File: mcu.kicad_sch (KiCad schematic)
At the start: 40 parts, among them J17 CAN, J19 Conn_ARM_JTAG_SWD_10, J20 Conn_ARM_JTAG_SWD_10, J21 Conn_01x04_Pin, SW1 RESET, SW2 BOOT, U17 HDC1080, U18 SN65HVD230, U8 STM32G473CBTx, Y1 8 MHz

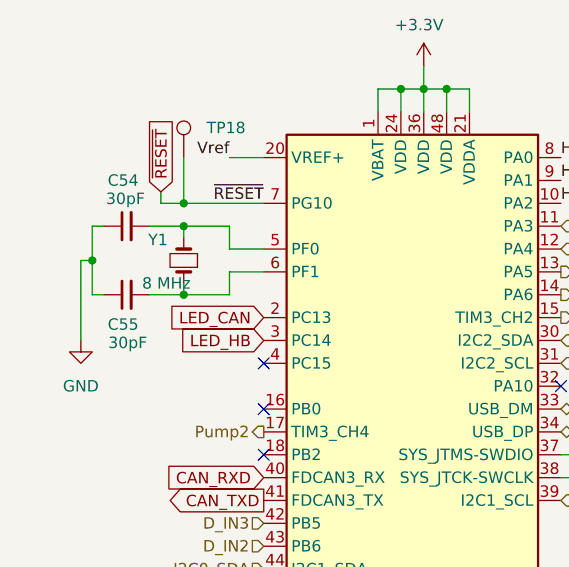
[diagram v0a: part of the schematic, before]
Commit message: Remove 8 MHz crystal
Closes #51
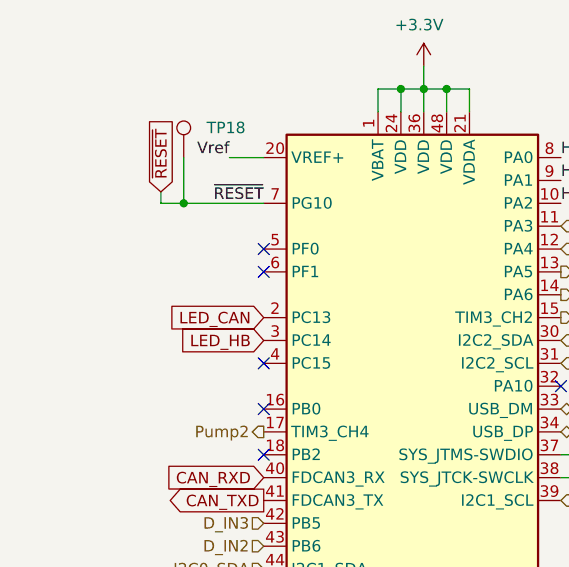
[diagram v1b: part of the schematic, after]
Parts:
- removed C54, C55: 30pF, Capacitor_SMD:C_0603_1608Metric, symbol Device:C_Small
- removed Y1: 8 MHz, Crystal:Crystal_SMD_5032-2Pin_5.0x3.2mm, symbol Device:Crystal_Small
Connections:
- no-connect marks 11 -> 13

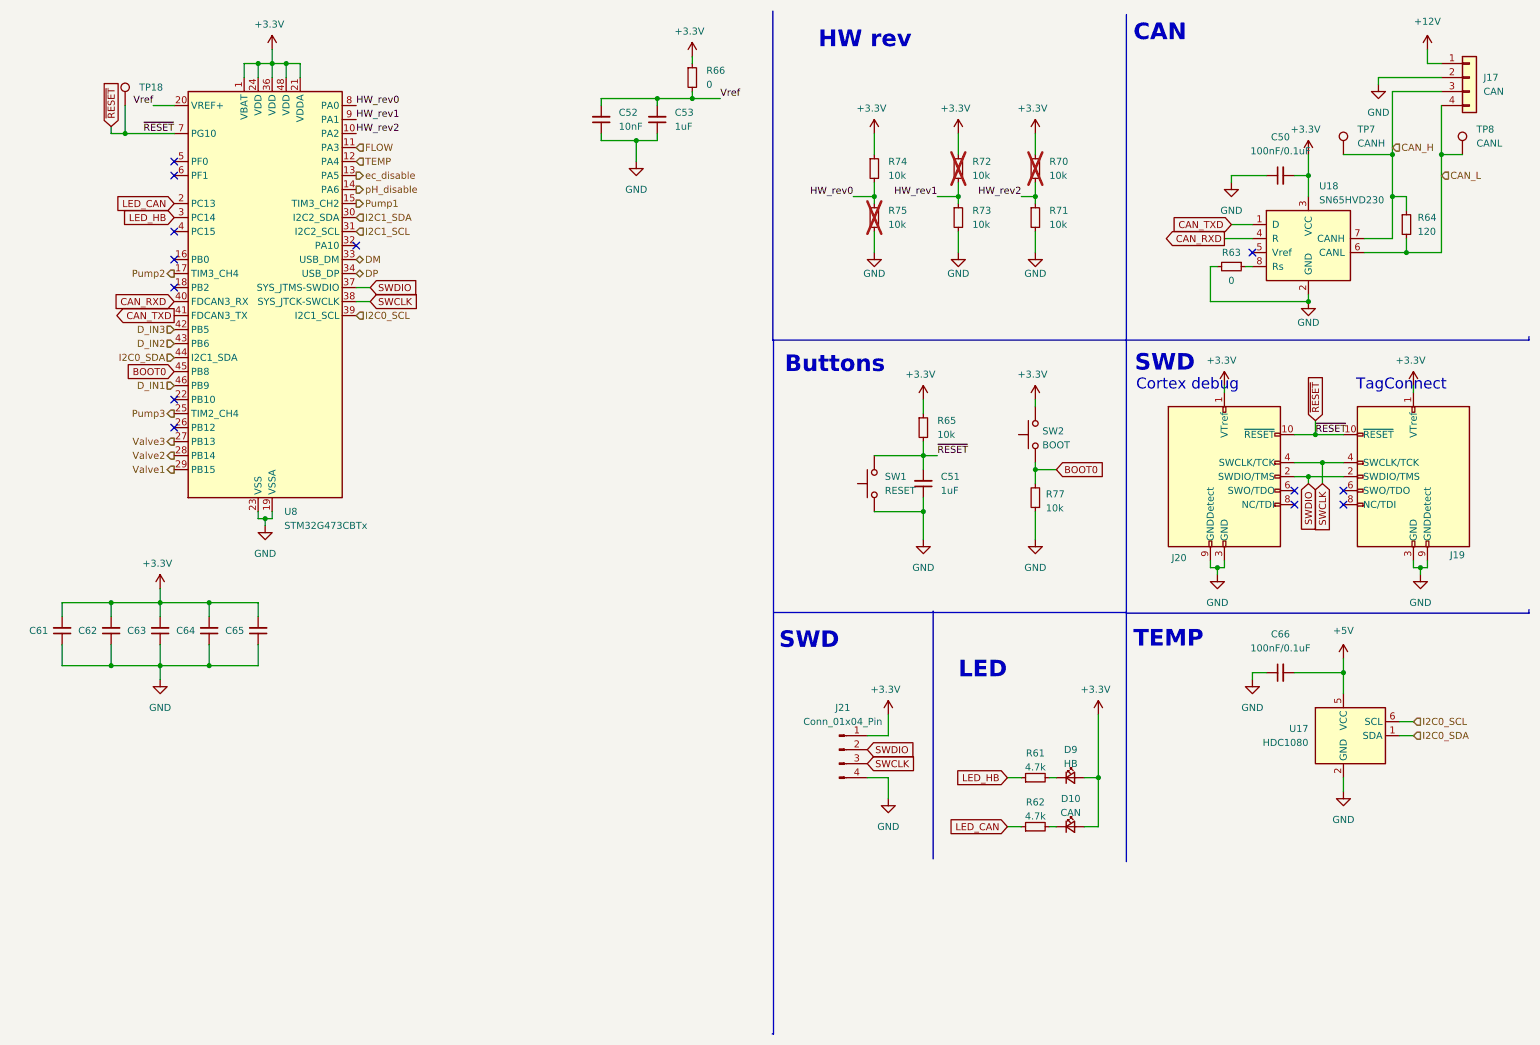
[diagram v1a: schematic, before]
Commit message: Replace MCU with STM32U575RGT
Closes #49
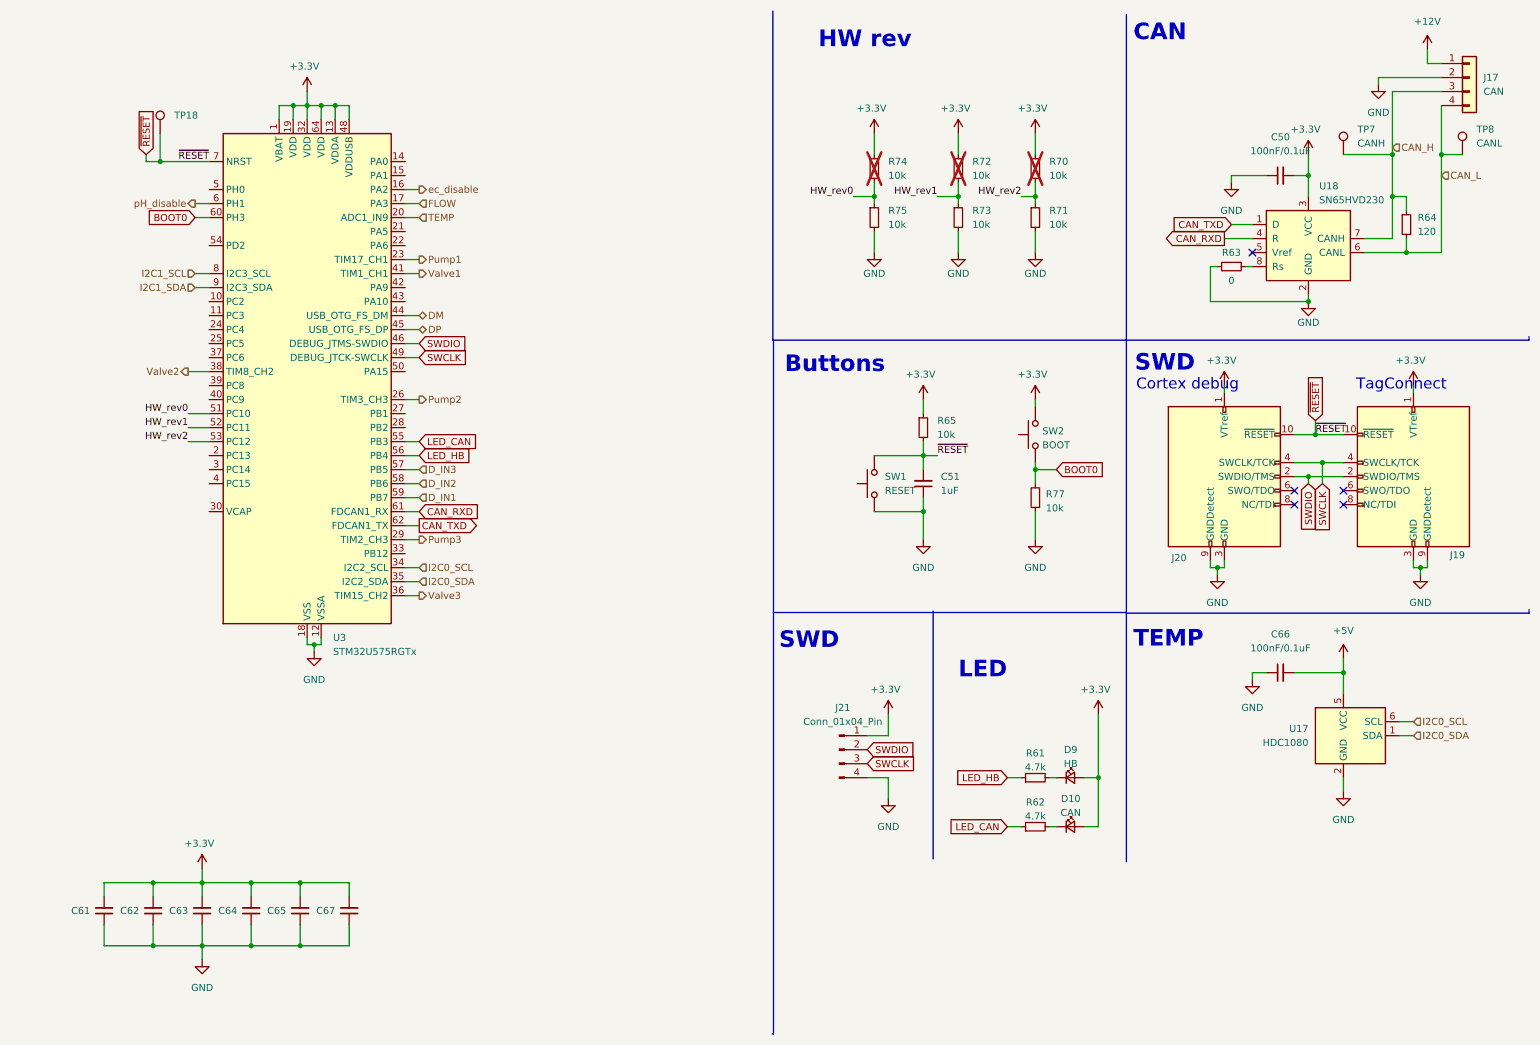
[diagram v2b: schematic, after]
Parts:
- removed C52: 10nF, Capacitor_SMD:C_0402_1005Metric, symbol Device:C_Small
- removed C53: 1uF, Capacitor_SMD:C_0402_1005Metric, symbol Device:C_Small
- removed R66: 0, Resistor_SMD:R_0402_1005Metric, symbol Device:R_Small
- removed U8: STM32G473CBTx, Package_QFP:LQFP-48_7x7mm_P0.5mm, symbol MCU_ST_STM32G4:STM32G473CBTx
- added C67: 100nF/0.1uF, Capacitor_SMD:C_0402_1005Metric, symbol Device:C_Small
- added U3: STM32U575RGTx, Package_QFP:LQFP-64_10x10mm_P0.5mm, symbol MCU_ST_STM32U5:STM32U575RGTx
- R74: now not fitted; now left out of the parts list
- R75: now fitted; now in the parts list
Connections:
- net +3.3V: now also C67.2, U3.1 (VBAT), U3.13 (VDDA), U3.19 (VDD), U3.32 (VDD), U3.48 (VDDUSB), U3.64 (VDD)
- net BOOT0: now also U3.60 (PH3)
- net CAN_RXD: now also U3.61 (PB8)
- net CAN_TXD: now also U3.62 (PB9)
- net DM: now also U3.44 (PA11)
- net DP: now also U3.45 (PA12)
- net D_IN1: now also U3.59 (PB7)
- net D_IN2: now also U3.58 (PB6)
- net D_IN3: now also U3.57 (PB5)
- net FLOW: now also U3.17 (PA3)
- net GND: now also C67.1, U3.12 (VSSA), U3.18 (VSS), U3.31 (VSS), U3.47 (VSS), U3.63 (VSS)
- net HW_rev0: now also U3.51 (PC10)
- net HW_rev1: now also U3.52 (PC11)
- net HW_rev2: now also U3.53 (PC12)
- net I2C0_SCL: now also U3.34 (PB13)
- net I2C0_SDA: now also U3.35 (PB14)
- net I2C1_SCL: now also U3.8 (PC0)
- net I2C1_SDA: now also U3.9 (PC1)
- net LED_CAN: now also U3.55 (PB3)
- net LED_HB: now also U3.56 (PB4)
- net Pump1: now also U3.23 (PA7)
- net Pump2: now also U3.26 (PB0)
- net Pump3: now also U3.29 (PB10)
- net SWCLK: now also U3.49 (PA14)
- net SWDIO: now also U3.46 (PA13)
- net TEMP: now also U3.20 (PA4)
- net Valve1: now also U3.41 (PA8)
- net Valve2: now also U3.38 (PC7)
- net Valve3: now also U3.36 (PB15)
- net ec_disable: now also U3.16 (PA2)
- net pH_disable: now also U3.6 (PH1)
- net ~{RESET}: now also U3.7 (NRST)
- no-connect marks 13 -> 5
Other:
- moved on the sheet: C61, C62, C63, C64, C65, TP18

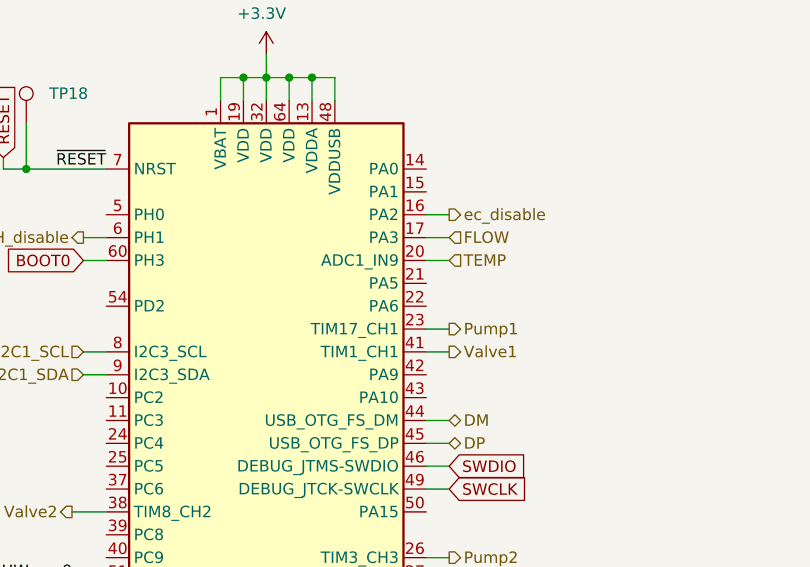
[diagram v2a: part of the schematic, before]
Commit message: Add Reverse polarity protection
Closes #55
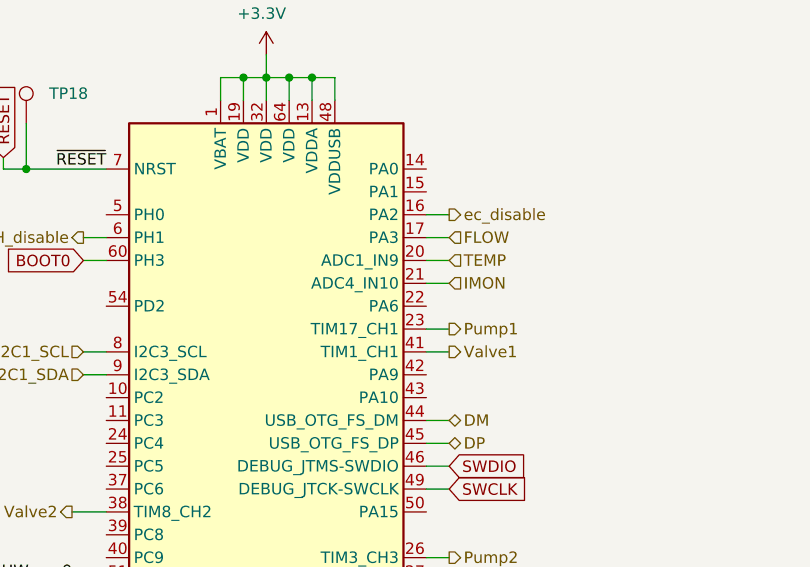
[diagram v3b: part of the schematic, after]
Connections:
- net IMON: now reaches U3.21 (PA5)
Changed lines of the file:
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@@
 	(wire
 		(pts
+			(xy 81.28 52.07) (xy 83.82 52.07)
+		)
+		(stroke
+			(width 0)
+			(type default)
+		)
+	)
+	(wire
+		(pts
 			(xy 269.24 29.21) (xy 269.24 38.1)
 		)
@@
 		)
 	)
+	(hierarchical_label "IMON"
+		(shape input)
+		(at 83.82 52.07 0)
+		(effects
+			(font
+				(size 1.27 1.27)
+			)
+			(justify left)
+		)
+	)
 	(hierarchical_label "Valve1"
 		(shape output)
@@
 		)
 		(pin "21"
-			(alternate "PA5")
+			(alternate "ADC4_IN10")
 		)
 		(pin "55"

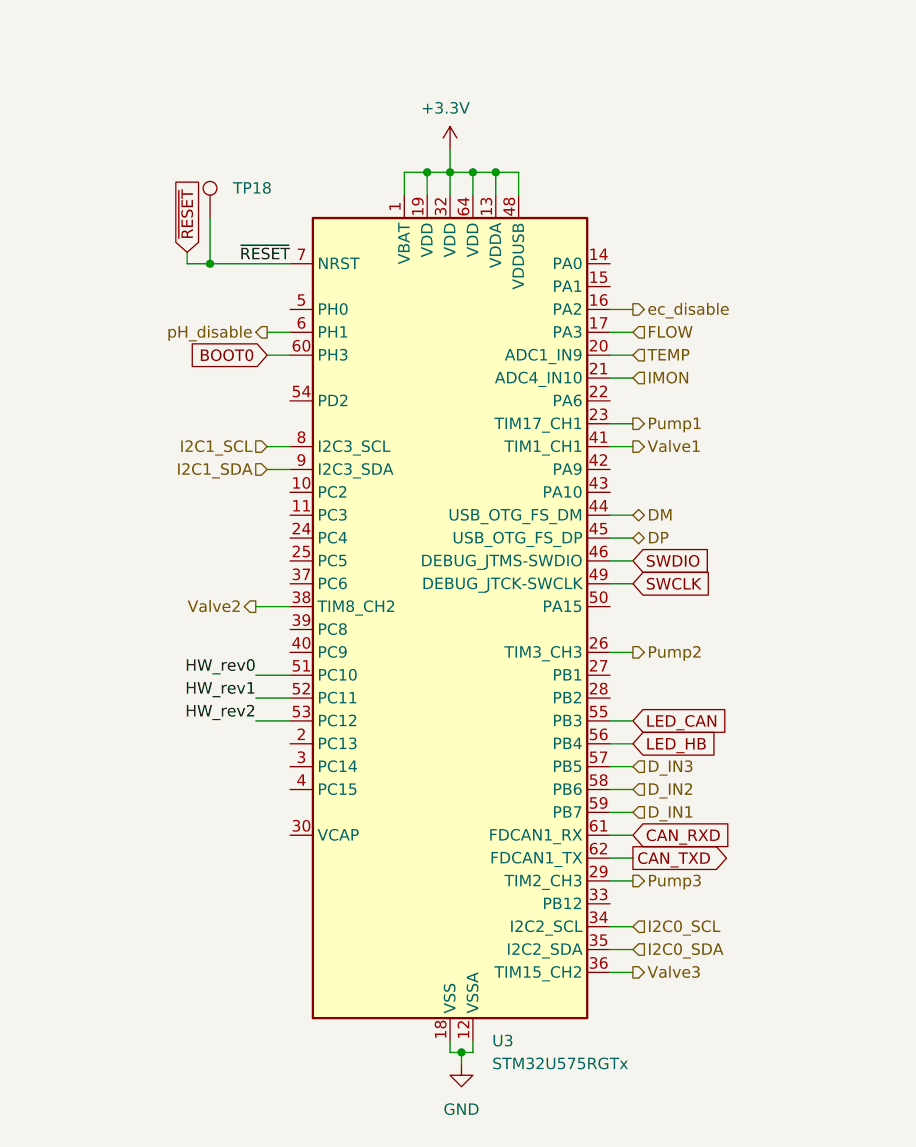
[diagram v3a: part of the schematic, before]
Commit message: Replace 4 of the 6 highside outputs with TPS4H160B
See #50
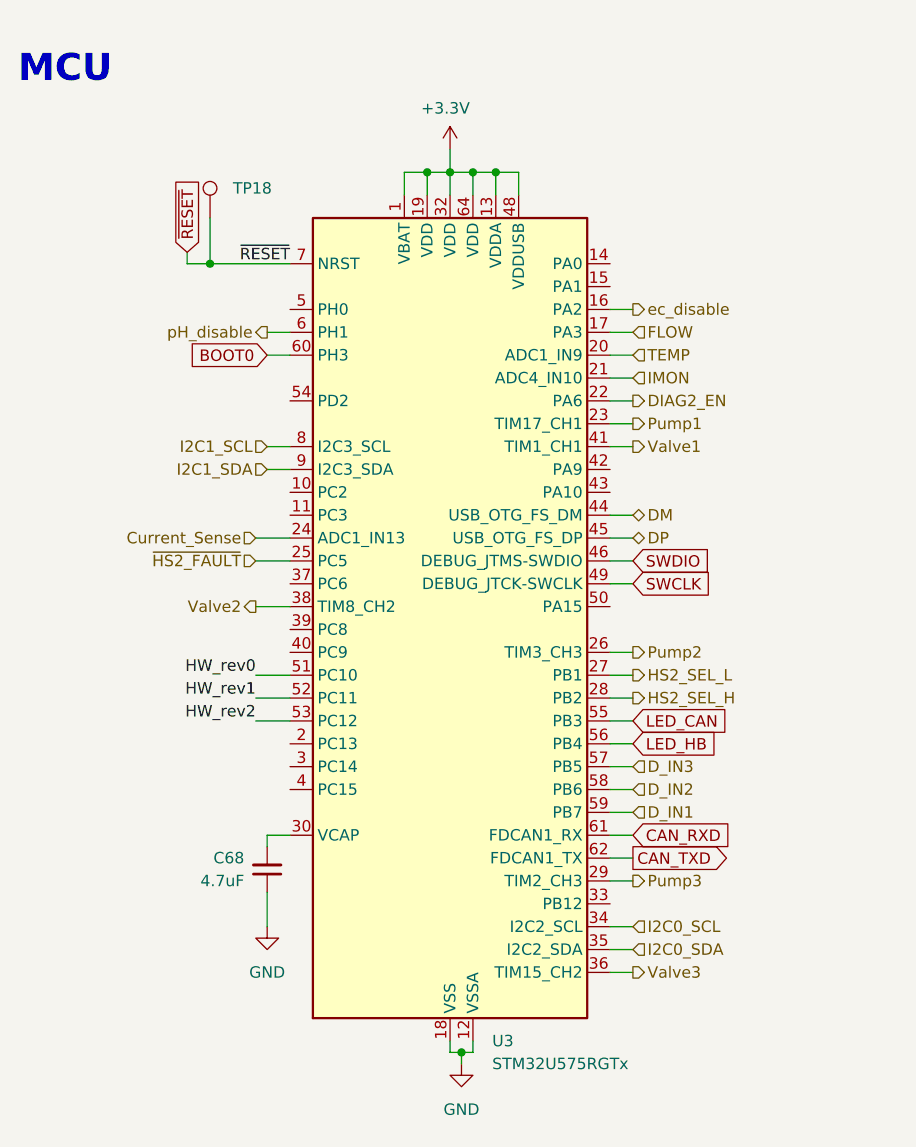
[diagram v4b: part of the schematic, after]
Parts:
- added C68: 4.7uF, Capacitor_SMD:C_0402_1005Metric, symbol Device:C_Small
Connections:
- net GND: now also C68.1
- net DIAG2_EN: now reaches U3.22 (PA6)
- net Current_Sense: now reaches U3.24 (PC4)
- net ~{HS2_FAULT}: now reaches U3.25 (PC5)
- net HS2_SEL_L: now reaches U3.27 (PB1)
- net HS2_SEL_H: now reaches U3.28 (PB2)
- net at U3.30 (VCAP): now also C68.2
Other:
- note added: "MCU"
